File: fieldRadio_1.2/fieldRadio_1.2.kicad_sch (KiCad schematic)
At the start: 12 parts, among them J1 Conn_01x02, J12 Conn_01x02, J18 Conn_01x16, J2 Conn_01x02, J3 Conn_01x03, J4 AudioJack2_Switch, J5 AudioJack3_Switch, J6 AudioJack2_Switch, J7 Conn_01x04, J8 Conn_01x12

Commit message: Starting to update fieldRadio 1.2 schematics
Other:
- added sheet HPLP Filters (hplp_filters.kicad_sch)

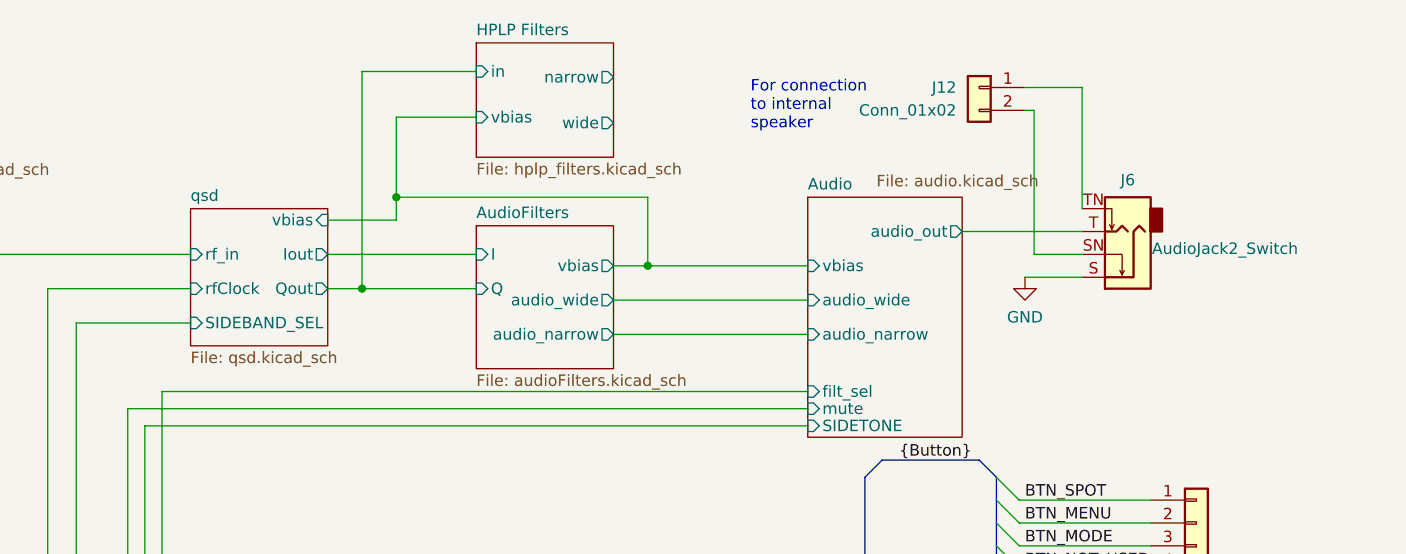
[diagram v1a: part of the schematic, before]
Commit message: schematic audio work on the audio path
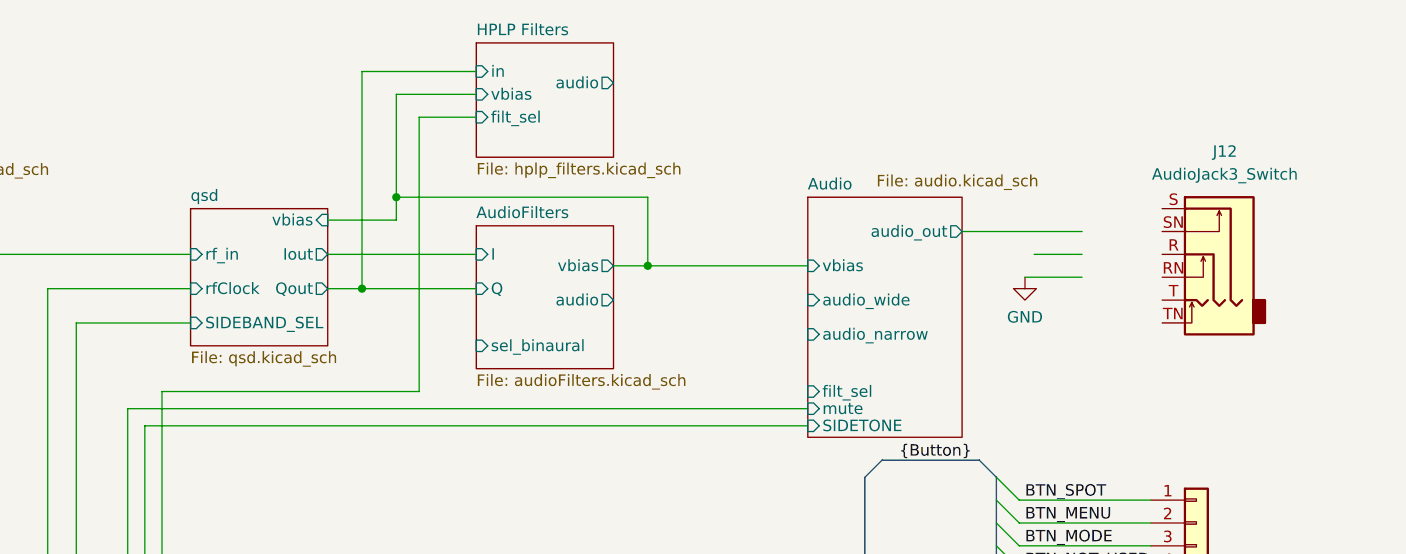
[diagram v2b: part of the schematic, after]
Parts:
- removed J12: Conn_01x02, Connector_PinHeader_2.54mm:PinHeader_1x02_P2.54mm_Vertical, symbol Connector_Generic:Conn_01x02
- removed J6: AudioJack2_Switch, Connector_Audio:Jack_6.35mm_Neutrik_NMJ4HFD3_Horizontal, symbol Connector_Audio:AudioJack2_Switch
- added J12: AudioJack3_Switch, Connector_Audio:Jack_6.35mm_Neutrik_NMJ6HFD2_Horizontal, symbol Connector_Audio:AudioJack3_Switch
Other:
- sheet AudioFilters ports: added audio, sel_binaural; removed audio_narrow, audio_wide
- sheet HPLP Filters ports: added audio, filt_sel; removed narrow, wide
- note removed: "For connection to internal speaker"
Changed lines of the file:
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@@
 		)
 	)
-	(text "For connection\nto internal\nspeaker"
-		(exclude_from_sim no)
-		(at 215.9 25.654 0)
-		(effects
-			(font
-				(size 1.27 1.27)
-			)
-			(justify left bottom)
-		)
-	)
 	(text "DB2"
 		(exclude_from_sim no)
@@
 	(wire
 		(pts
-			(xy 200.66 48.26) (xy 222.25 48.26)
-		)
-		(stroke
-			(width 0)
-			(type default)
-		)
-	)
-	(wire
-		(pts
 			(xy 171.45 119.38) (xy 94.615 119.38)
 		)
@@
 	(wire
 		(pts
-			(xy 200.66 44.45) (xy 222.25 44.45)
-		)
-		(stroke
-			(width 0)
-			(type default)
-		)
-	)
-	(wire
-		(pts
 			(xy 250.825 102.87) (xy 269.875 102.87)
 		)
@@
 		)
 	)
-	(bus
+	(wire
 		(pts
-			(xy 28.575 50.8) (xy 28.575 53.34)
+			(xy 185.42 24.13) (xy 179.07 24.13)
 		)
 		(stroke
@@
 	(bus
 		(pts
-			(xy 107.95 49.53) (xy 107.95 52.07)
+			(xy 28.575 50.8) (xy 28.575 53.34)
 		)
 		(stroke
@@
 		)
 	)
-	(wire
+	(bus
 		(pts
-			(xy 176.53 24.13) (xy 176.53 33.02)
+			(xy 107.95 49.53) (xy 107.95 52.07)
 		)
 		(stroke
@@
 	(wire
 		(pts
-			(xy 252.73 20.828) (xy 252.73 34.29)
+			(xy 176.53 21.59) (xy 176.53 33.02)
 		)
 		(stroke
@@
 	(wire
 		(pts
-			(xy 150.495 54.61) (xy 222.25 54.61)
+			(xy 150.495 54.61) (xy 179.07 54.61)
 		)
 		(stroke
@@
 	(wire
 		(pts
-			(xy 247.396 39.37) (xy 247.396 23.368)
-		)
-		(stroke
-			(width 0)
-			(type default)
-		)
-	)
-	(wire
-		(pts
 			(xy 185.42 19.05) (xy 172.72 19.05)
 		)
@@
 	(wire
 		(pts
-			(xy 246.38 20.828) (xy 252.73 20.828)
-		)
-		(stroke
-			(width 0)
-			(type default)
-		)
-	)
-	(wire
-		(pts
 			(xy 226.06 88.265) (xy 212.09 88.265)
 		)
@@
 	(wire
 		(pts
-			(xy 247.396 23.368) (xy 246.38 23.368)
-		)
-		(stroke
-			(width 0)
-			(type default)
-		)
-	)
-	(wire
-		(pts
 			(xy 148.59 125.73) (xy 148.59 58.42)
 		)
@@
 	(wire
 		(pts
+			(xy 179.07 24.13) (xy 179.07 54.61)
+		)
+		(stroke
+			(width 0)
+			(type default)
+		)
+	)
+	(wire
+		(pts
 			(xy 212.09 120.65) (xy 229.235 120.65)
 		)
@@
 	(wire
 		(pts
-			(xy 185.42 24.13) (xy 176.53 24.13)
+			(xy 185.42 21.59) (xy 176.53 21.59)
 		)
 		(stroke
@@
 	)
 	(symbol
-		(lib_id "Connector_Audio:AudioJack2_Switch")
-		(at 257.81 36.83 180)
-		(unit 1)
-		(exclude_from_sim no)
-		(in_bom yes)
-		(on_board yes)
-		(dnp no)
-		(property "Reference" "J6"
-			(at 257.81 31.115 0)
-			(effects
-				(font
-					(size 1.27 1.27)
-				)
-			)
-		)
-		(property "Value" "AudioJack2_Switch"
-			(at 268.605 38.735 0)
-			(effects
-				(font
-					(size 1.27 1.27)
-				)
-			)
-		)
-		(property "Footprint" "Connector_Audio:Jack_6.35mm_Neutrik_NMJ4HFD3_Horizontal"
-			(at 257.81 41.91 0)
-			(effects
-				(font
-					(size 1.27 1.27)
-				)
-				(hide yes)
-			)
-		)
-		(property "Datasheet" "~"
-			(at 257.81 41.91 0)
-			(effects
-				(font
-					(size 1.27 1.27)
-				)
-				(hide yes)
-			)
-		)
-		(property "Description" ""
-			(at 257.81 36.83 0)
-			(effects
-				(font
-					(size 1.27 1.27)
-				)
-			)
-		)
-		(property "Mouser Part Number" "568-NMJ4HFD3"
-			(at 257.81 36.83 0)
-			(effects
-				(font
-					(size 1.27 1.27)
-				)
-				(hide yes)
-			)
-		)
-		(pin "S"
-		)
-		(pin "SN"
-		)
-		(pin "T"
-		)
-		(pin "TN"
-		)
-		(instances
-			(project "fieldRadio_1.2"
-				(path "/a1d1b2b0-2f27-4dc0-94ba-bb0e02933617"
-					(reference "J6")
-					(unit 1)
-				)
-			)
-		)
-	)
-	(symbol
 		(lib_id "Connector_Generic:Conn_01x12")
 		(at 265.43 79.375 0)
@@
 	)
 	(symbol
+		(lib_id "Connector_Audio:AudioJack3_Switch")
+		(at 266.7 39.37 0)
+		(mirror y)
+		(unit 1)
+		(exclude_from_sim no)
+		(in_bom yes)
+		(on_board yes)
+		(dnp no)
+		(property "Reference" "J12"
+			(at 268.605 27.94 0)
+			(effects
+				(font
+					(size 1.27 1.27)
+				)
+			)
+		)
+		(property "Value" "AudioJack3_Switch"
+			(at 268.605 30.48 0)
+			(effects
+				(font
+					(size 1.27 1.27)
+				)
+			)
+		)
+		(property "Footprint" "Connector_Audio:Jack_6.35mm_Neutrik_NMJ6HFD2_Horizontal"
+			(at 266.7 39.37 0)
+			(effects
+				(font
+					(size 1.27 1.27)
+				)
+				(hide yes)
+			)
+		)
+		(property "Datasheet" "~"
+			(at 266.7 39.37 0)
+			(effects
+				(font
+					(size 1.27 1.27)
+				)
+				(hide yes)
+			)
+		)
+		(property "Description" ""
+			(at 266.7 39.37 0)
+			(effects
+				(font
+					(size 1.27 1.27)
+				)
+			)
+		)
+		(property "Mouser Part Number" "550-20301"
+			(at 266.7 39.37 0)
+			(effects
+				(font
+					(size 1.27 1.27)
+				)
+				(hide yes)
+			)
+		)
+		(pin "RN"
+		)
+		(pin "TN"
+		)
+		(pin "T"
+		)
+		(pin "S"
+		)
+		(pin "SN"
+		)
+		(pin "R"
+		)
+		(instances
+			(project "fieldRadio_1.2"
+				(path "/a1d1b2b0-2f27-4dc0-94ba-bb0e02933617"
+					(reference "J12")
+					(unit 1)
+				)
+			)
+		)
+	)
+	(symbol
 		(lib_id "Connector_Generic:Conn_01x02")
 		(at 38.1 22.86 0)
@@
 		)
 	)
-	(symbol
-		(lib_id "Connector_Generic:Conn_01x02")
-		(at 241.3 20.828 0)
-		(mirror y)
-		(unit 1)
-		(exclude_from_sim no)
-		(in_bom yes)
-		(on_board yes)
-		(dnp no)
-		(property "Reference" "J12"
-			(at 238.76 20.828 0)
-			(effects
-				(font
-					(size 1.27 1.27)
-				)
-				(justify left)
-			)
-		)
-		(property "Value" "Conn_01x02"
-			(at 238.76 23.368 0)
-			(effects
-				(font
-					(size 1.27 1.27)
-				)
-				(justify left)
-			)
-		)
-		(property "Footprint" "Connector_PinHeader_2.54mm:PinHeader_1x02_P2.54mm_Vertical"
-			(at 241.3 20.828 0)
-			(effects
-				(font
-					(size 1.27 1.27)
-				)
-				(hide yes)
-			)
-		)
-		(property "Datasheet" "~"
-			(at 241.3 20.828 0)
-			(effects
-				(font
-					(size 1.27 1.27)
-				)
-				(hide yes)
-			)
-		)
-		(property "Description" ""
-			(at 241.3 20.828 0)
-			(effects
-				(font
-					(size 1.27 1.27)
-				)
-			)
-		)
-		(property "Mouser Part Number" ""
-			(at 241.3 20.828 0)
-			(effects
-				(font
-					(size 1.27 1.27)
-				)
-				(hide yes)
-			)
-		)
-		(pin "2"
-		)
-		(pin "1"
-		)
-		(instances
-			(project "fieldRadio_1.2"
-				(path "/a1d1b2b0-2f27-4dc0-94ba-bb0e02933617"
-					(reference "J12")
-					(unit 1)
-				)
-			)
-		)
-	)
 	(sheet
 		(at 64.77 36.195)
@@
 			)
 		)
-		(pin "narrow" output
-			(at 200.66 19.685 0)
+		(pin "in" input
+			(at 185.42 19.05 180)
 			(effects
 				(font
 					(size 1.27 1.27)
 				)
-				(justify right)
+				(justify left)
 			)
 		)
-		(pin "wide" output
-			(at 200.66 24.765 0)
+		(pin "vbias" input
+			(at 185.42 21.59 180)
 			(effects
 				(font
 					(size 1.27 1.27)
 				)
-				(justify right)
+				(justify left)
 			)
 		)
-		(pin "in" input
-			(at 185.42 19.05 180)
+		(pin "filt_sel" input
+			(at 185.42 24.13 180)
 			(effects
 				(font
@@
 			)
 		)
-		(pin "vbias" input
-			(at 185.42 24.13 180)
+		(pin "audio" output
+			(at 200.66 20.32 0)
 			(effects
 				(font
 					(size 1.27 1.27)
 				)
-				(justify left)
+				(justify right)
 			)
 		)
@@
 			)
 		)
-		(pin "audio_wide" output
-			(at 200.66 44.45 0)
+		(pin "sel_binaural" input
+			(at 185.42 49.53 180)
 			(effects
 				(font
 					(size 1.27 1.27)
 				)
-				(justify right)
+				(justify left)
 			)
 		)
-		(pin "audio_narrow" output
-			(at 200.66 48.26 0)
+		(pin "audio" output
+			(at 200.66 44.45 0)
 			(effects
 				(font
